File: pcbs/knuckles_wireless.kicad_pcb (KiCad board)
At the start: 2 copper layers, 130.3 x 107.9 mm, 120 parts

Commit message: fix(pcb): persist kicad project settings
Store the wireless KiCad design rules outside generated output and sync
them after each Ergogen run. This preserves the 0.25 mm JLCPCB edge
clearance.

Also correct the wireless PCB filename and embedded labels so tooling
consistently uses `knuckles`.
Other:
- board text added: "knuckles v1.0"
- board text removed: "knucles v1.0"
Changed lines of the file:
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@@
   (paper "A3")
   (title_block
-    (title "knucles_wireless")
+    (title "knuckles_wireless")
     (date "2025-03-17")
     (rev "0.2")
@@
   (segment (start 215.90430500000002 86.635) (end 215.303695 86.635) (width 0.25) (layer "B.Cu"))
   (segment (start 215.303695 86.635) (end 214.798695 87.14) (width 0.25) (layer "B.Cu"))
-  (gr_text "knucles v1.0"
+  (gr_text "knuckles v1.0"
     (at 137 107.4 0)
     (layer "F.SilkS" )
@@
     )
   )
-  (gr_text "knucles v1.0"
+  (gr_text "knuckles v1.0"
     (at 137 107.4 0)
     (layer "B.SilkS" )

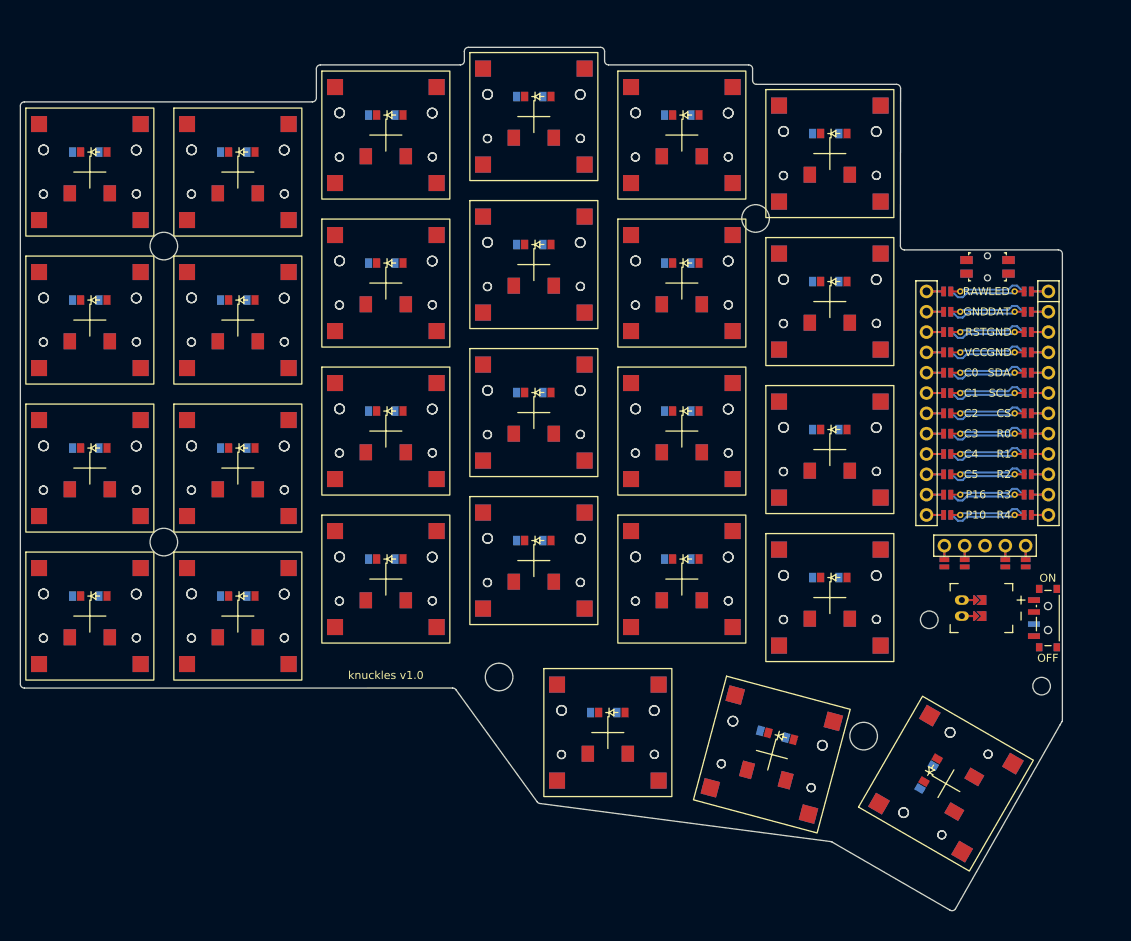
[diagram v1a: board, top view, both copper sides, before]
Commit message: fix(pcb): increase key spacing and correct power switch
Set the PG1316S key pitch to 19.5 mm in both axes and regenerate the tracked PCB and outline artifacts.

Keep the power switch mapping consistent with the intended on/off orientation while preserving the original board outline.
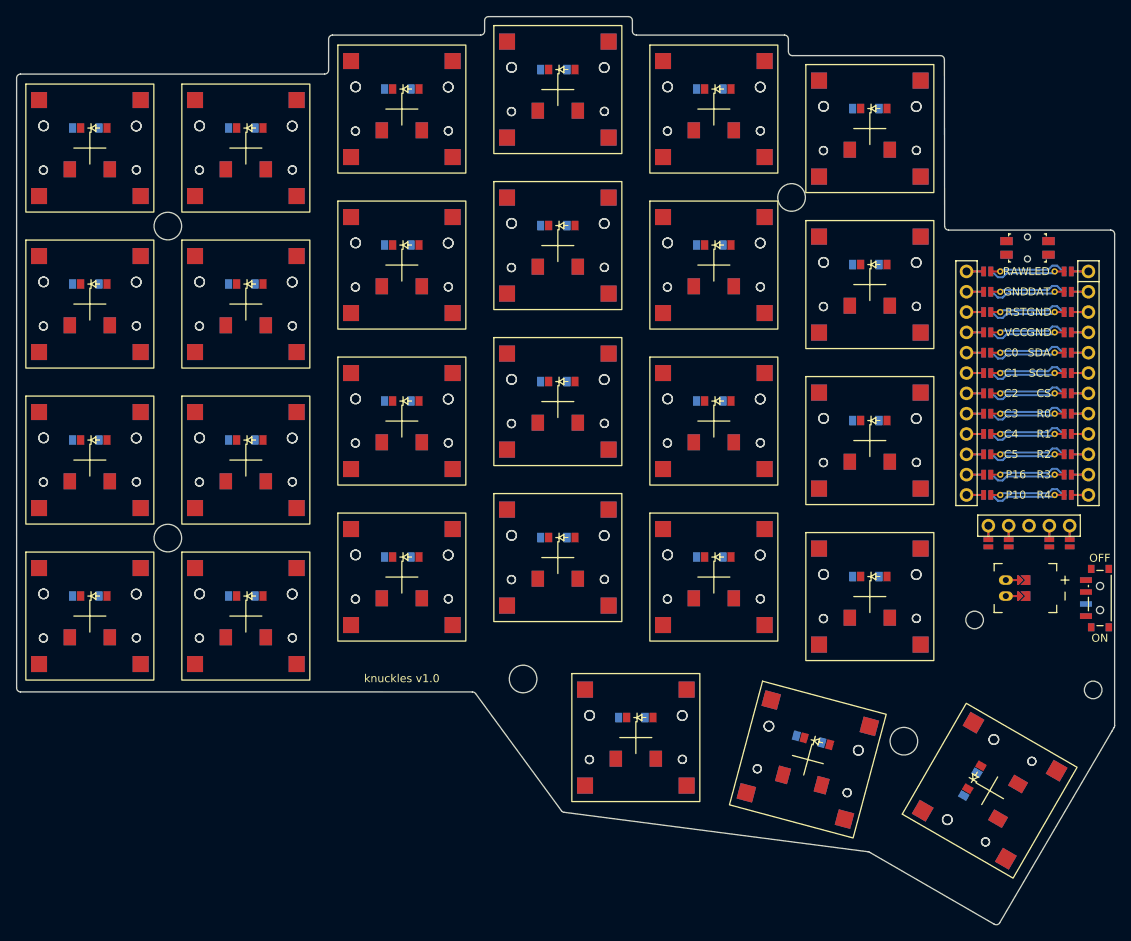
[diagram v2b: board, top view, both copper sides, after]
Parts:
- moved PWR1 6.96 mm to (226.2, 97.8)
- moved MH2 6.47 mm to (225.4, 109.2)
- moved DISP1 6.04 mm to (217.4, 72.0)
- moved JST1 6.04 mm to (214.5, 96.5)
- moved D24 5.90 mm to (197.0, 36.6)
- moved D51 5.90 mm to (198.0, 36.6)
- moved S24 5.90 mm to (197.5, 39.1)
- moved S51 5.90 mm to (197.5, 39.1)
- moved MH1 5.67 mm to (210.6, 100.5)
- moved MCU1 5.59 mm to (217.2, 69.6)
- moved D27 5.54 mm to (210.1, 121.0)
- moved D54 5.54 mm to (210.6, 120.1)
- moved S27 5.54 mm to (212.5, 121.8)
- moved S54 5.54 mm to (212.5, 121.8)
- moved RST1 5.53 mm to (217.2, 54.0)
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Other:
- board size 130.3 x 107.9 mm -> 137.3 x 113.5 mm
